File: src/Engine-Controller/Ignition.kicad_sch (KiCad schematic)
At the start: 9 parts, among them P8 Solid Prop Cont, Q1 QS5U17TR

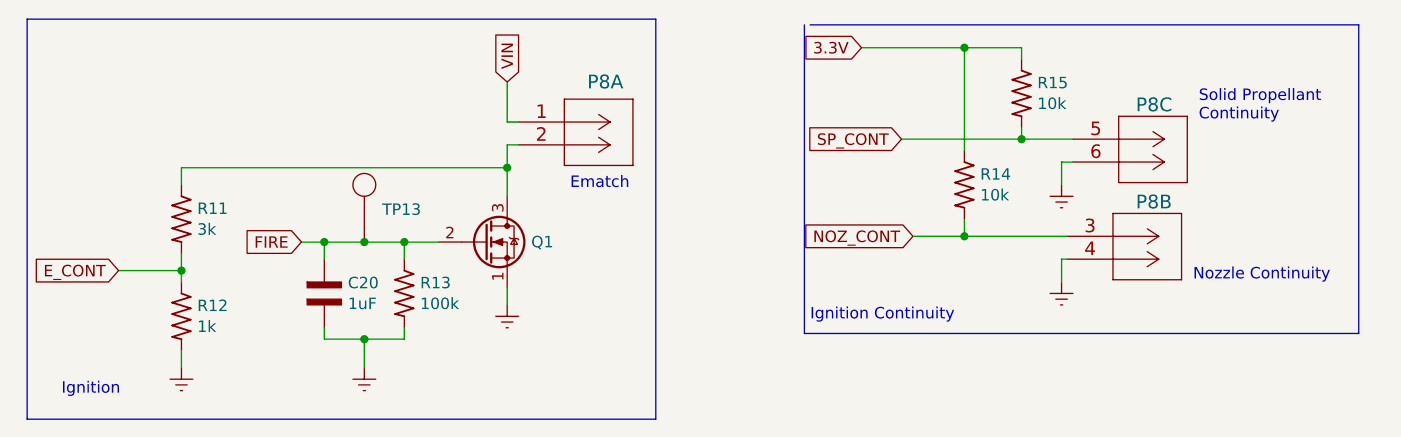
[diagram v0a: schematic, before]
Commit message: Removed misc elements from connectors sheet
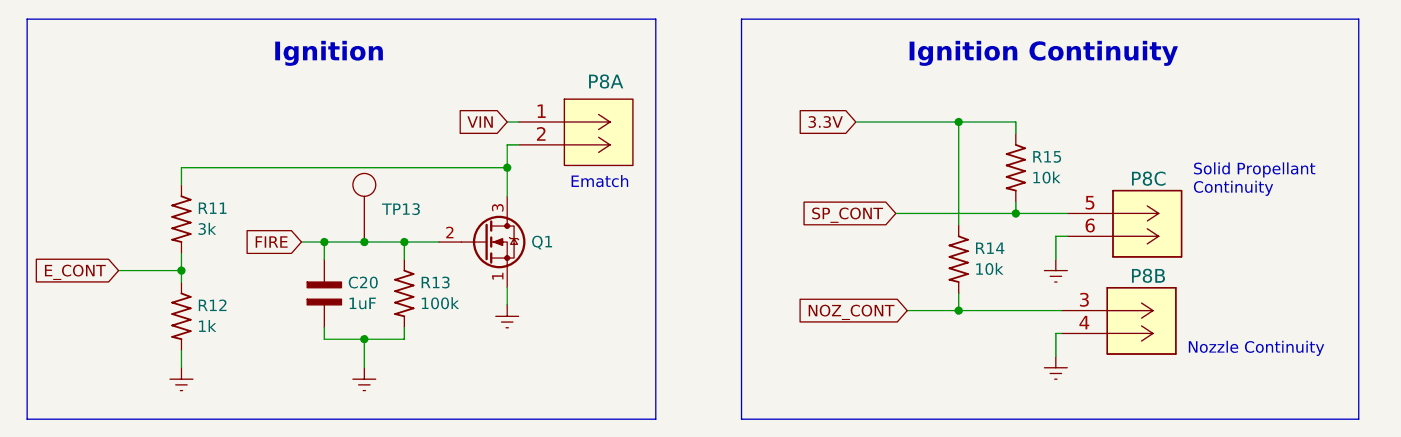
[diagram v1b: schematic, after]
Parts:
- P8: footprint Engine-Controller:TE_282837-6 -> 66953-005LF_AMP
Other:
- moved on the sheet: R14, R15
